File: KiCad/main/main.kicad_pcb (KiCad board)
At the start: 2 copper layers, 88 x 90.3 mm, 39 parts, among them J1 Hexpansion-Connector, J2 Conn_01x04_Socket, U1 TCA8418, U2 AP3032AKTR, U4 ZD24C64A-XGMT

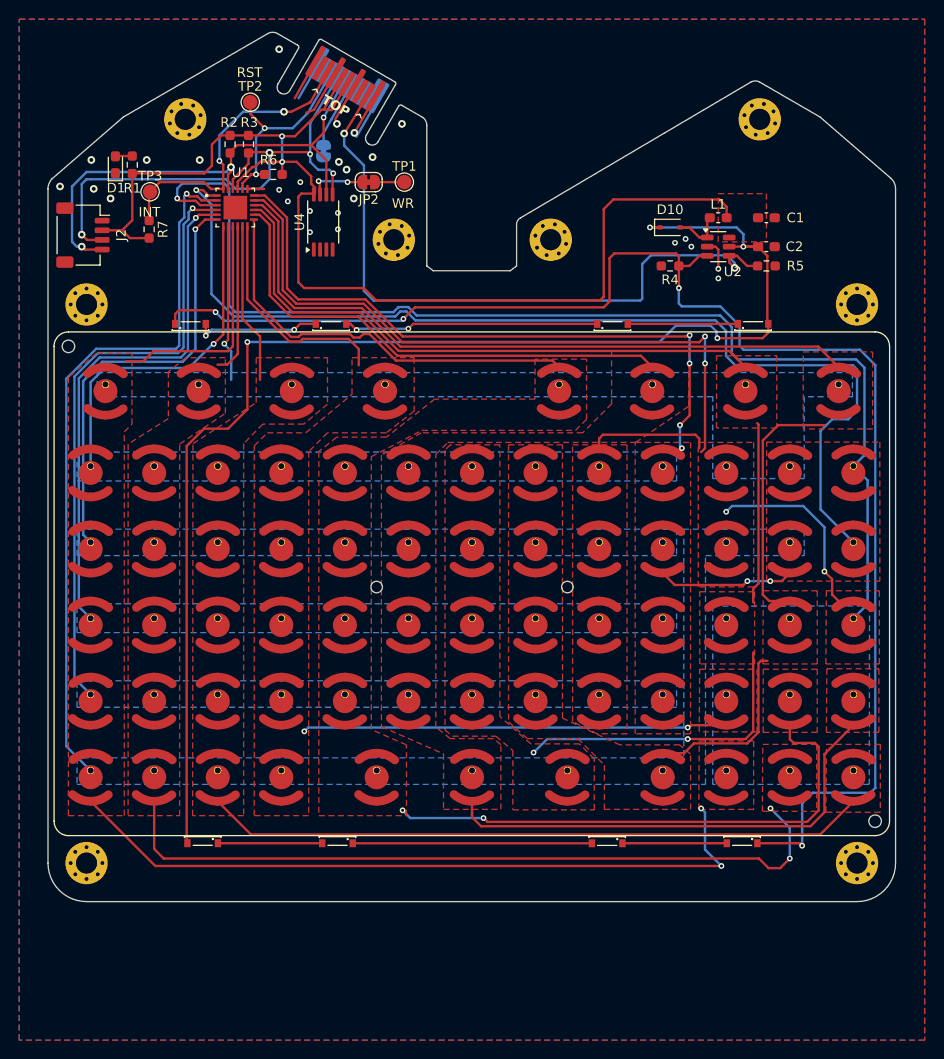
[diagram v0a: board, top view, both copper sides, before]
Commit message: Modify for EMF camp - Change shape - Move standoffs to bottom PCB - Add RGB LEDs and power conversion for them - Add art - Generate and add 3D models
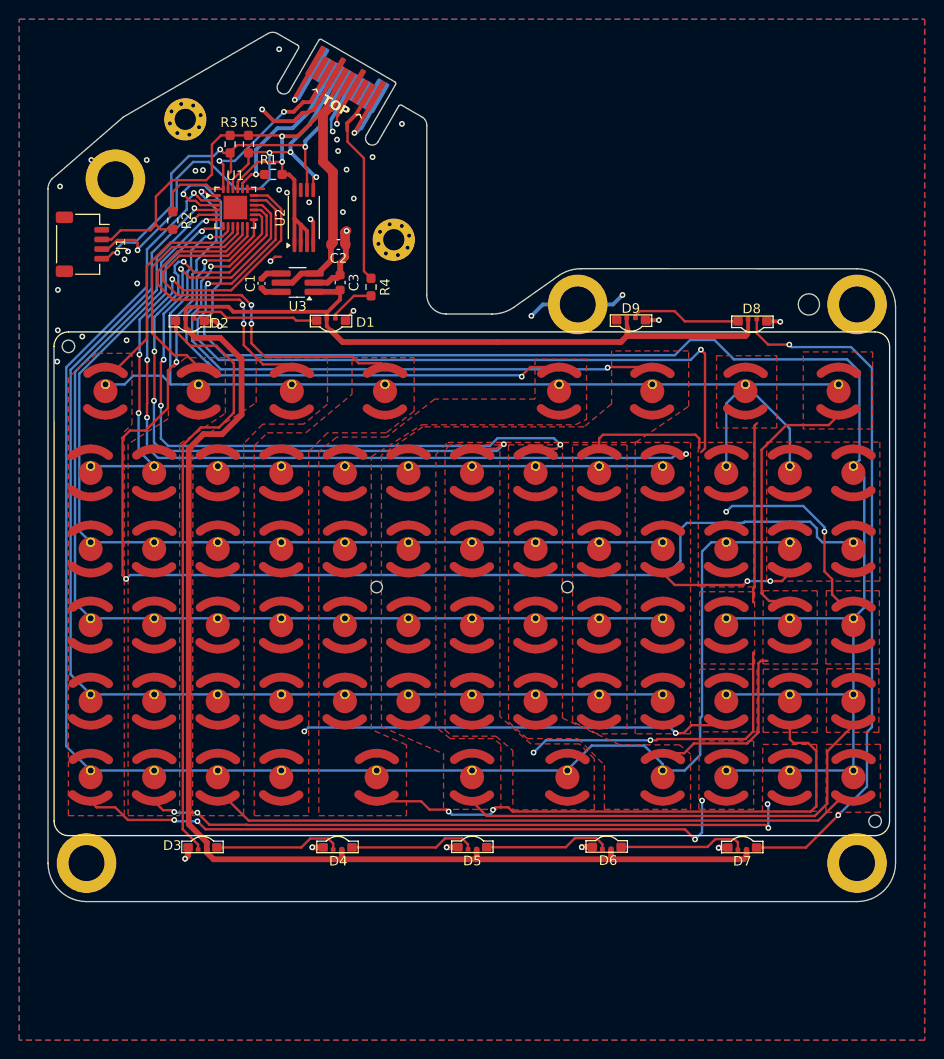
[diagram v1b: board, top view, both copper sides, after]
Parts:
- removed D10: 1N5819WS, Diode_SMD:D_SOD-323
- removed the H3 at (8.20, -35.7)
- removed H8: MountingHole_Pad, MountingHole:MountingHole_2.2mm_M2_Pad_Via
- removed JP1, JP2: SolderJumper_2_Bridged, Jumper:SolderJumper-2_P1.3mm_Bridged_RoundedPad1.0x1.5mm
- removed L1: 6.8uH, Inductor_SMD:L_0603_1608Metric_Pad1.05x0.95mm_HandSolder
- removed the R1 at (-35.2, -43.5)
- removed the R5 at (30.6, -33.0)
- removed TP1, TP2, TP3: TestPoint, TestPoint:TestPoint_Pad_D1.5mm
- removed the U2 at (25.6, -35.0)
- added C3: 10uF, Capacitor_SMD:C_0603_1608Metric, F.Cu at (-13.7, -31.3)
- added H2: SMTSO2020CTJ, frontplate:SMTSO2020CTJ, F.Cu at (11.0, -29.0)
- added U3: AP3602A, Package_TO_SOT_SMD:TSOT-23-6_HandSoldering, F.Cu at (-18.1, -31.3)
- C1: value 10uF -> 1uF; footprint Capacitor_SMD:C_0603_1608Metric_Pad1.08x0.95mm_HandSolder -> Capacitor_SMD:C_0402_1005Metric
- C2: value 1uF -> 10uF; footprint Capacitor_SMD:C_0603_1608Metric_Pad1.08x0.95mm_HandSolder -> Capacitor_SMD:C_0603_1608Metric
- D1: value LED -> XL-3210RGBC-WS2812B; footprint LED_SMD:LED_0603_1608Metric_Pad1.05x0.95mm_HandSolder -> tildagon:XL-3210RGBC-2812B
- D2, D3, D4, D5, D6, D7, D8, D9: value LED -> XL-3210RGBC-WS2812B; footprint keyboard_leds:LTW-010DCG -> tildagon:XL-3210RGBC-2812B
- H4, H5, H6, H7: value MountingHole_Pad -> SMTSO2020CTJ; footprint MountingHole:MountingHole_2.2mm_M2_Pad_Via -> frontplate:SMTSO2020CTJ
- R4: value 20R -> 3k3
- U1: footprint TCA8418RTWR:QFN50P400X400X80-25N -> Package_DFN_QFN:WQFN-24-1EP_4x4mm_P0.5mm_EP2.45x2.45mm
- moved H6 98.8 mm to (-40.0, 29.0)
- moved H5 80.0 mm to (40.0, -29.0)
- moved D9 70.1 mm to (16.5, -27.4)
- moved D8 69.2 mm to (29.1, -27.2)
- moved H4 67.2 mm to (-37.0, -42.0), turned to 0 degrees
- moved D5 61.6 mm to (0.06, 27.4)
- moved D4 61.3 mm to (-13.9, 27.4)
- moved D3 55.9 mm to (-28.0, 27.4)
- moved C1 52.9 mm to (-21.8, -31.2), turned to 90 degrees
- moved C2 44.4 mm to (-13.8, -35.2), turned to 180 degrees
- moved R4 31.1 mm to (-10.5, -30.8), turned to 90 degrees
- moved D1 27.6 mm to (-14.6, -27.3), turned to 180 degrees
- moved D6 14.1 mm to (14.0, 27.3), turned to 0 degrees
- moved D7 14.0 mm to (28.1, 27.4), turned to 0 degrees
- moved R2 2.63 mm to (-31.0, -37.7)
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- renumbered H2 to H3, J2 to J1, J1 to J2, R6 to R1, R7 to R2, R2 to R3, R3 to R5, U4 to U2
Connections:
- C1 pad 1: VCC -> Net-(U3-C+)
- C1 pad 2: GND -> Net-(U3-C-)
- C2 pad 1: VDD -> GND
- C2 pad 2: GND -> VCC
- D1 pad 2: Net-(D1-A) -> Net-(D1-DIN)
- D2 pad 1: Net-(D2-K) -> GND
- D2 pad 2: Net-(D2-A) -> Net-(D1-DOUT)
- D3 pad 1: Net-(D2-A) -> GND
- D3 pad 2: Net-(D3-A) -> Net-(D2-DOUT)
- D4 pad 1: Net-(D3-A) -> GND
- D4 pad 2: Net-(D4-A) -> Net-(D3-DOUT)
- D5 pad 1: Net-(D4-A) -> GND
- D5 pad 2: VDD -> Net-(D4-DOUT)
- D6 pad 1: Net-(D2-K) -> GND
- D6 pad 2: Net-(D6-A) -> Net-(D5-DOUT)
- D7 pad 1: Net-(D6-A) -> GND
- D7 pad 2: Net-(D7-A) -> Net-(D6-DOUT)
- D8 pad 1: Net-(D7-A) -> GND
- D8 pad 2: Net-(D8-A) -> Net-(D7-DOUT)
- D9 pad 1: Net-(D8-A) -> GND
- D9 pad 2: VDD -> Net-(D8-DOUT)
- J2 pad 12: LED_CTRL -> /LED_DATA
- J2 pad 6: Net-(J1-HEXP_DET) -> GND
- R4 pad 1: Net-(D2-K) -> Net-(D1-DIN)
- R4 pad 2: GND -> /LED_DATA
- U2 pad 1: unconnected-(U4-A0-Pad1) -> VCC
- U2 pad 2: unconnected-(U4-A1-Pad2) -> VCC
- U2 pad 3: unconnected-(U4-A2-Pad3) -> VCC
- U2 pad 7: Net-(JP2-B) -> unconnected-(U2-WP-Pad7)
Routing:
- net /5V: track 0.00 -> 195.1 mm
- net Net-(D2-K): track 153.5 -> 0.00 mm, vias 4 -> 0
- net VDD: track 137.4 -> 0.00 mm, vias 4 -> 0
- net /ROW0: track 16.4 -> 116.5 mm
- net /ROW5: track 74.4 -> 166.4 mm
- net Net-(D7-DOUT): track 0.00 -> 72.7 mm, vias 0 -> 2
- net LED_CTRL: track 70.5 -> 0.00 mm, vias 2 -> 0
- net Net-(D2-DOUT): track 0.00 -> 63.0 mm
- net /ROW2: track 45.1 -> 100.1 mm
- net /ROW6: track 121.8 -> 176.7 mm
- net /ROW3: track 54.4 -> 109.1 mm
- net /ROW4: track 63.7 -> 118.5 mm
- net /ROW1: track 35.8 -> 89.9 mm, vias 1 -> 3
- net GND: track 32.3 -> 75.4 mm, vias 26 -> 43
- net VCC: track 125.7 -> 88.1 mm
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- removed copper zone on B.Cu, net /ROW0
- removed copper zone on B.Cu, net /ROW1
- removed copper zone on B.Cu, net /ROW2
- removed copper zone on B.Cu, net /ROW3
- removed copper zone on B.Cu, net /ROW4
- removed copper zone on B.Cu, net /ROW5
- removed copper zone on B.Cu, net /ROW6
- removed copper zone on F.Cu, net VCC
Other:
- outline, holes or cut-outs redrawn
- board text added: "Design by davedarko"
- board text added: "Designed for EMF Camp 2026"
- board text added: "Keeb"
- board text added: "Keypad by Solder Party"
- board text added: "Layout by Kliment"
- board text added: "PCB and assembly:"
- board text added: "Software by sodoku"
- board text added: "TCA8418 by:"
- board text added: "Tildagon"
- board text added: "dex"
- board text added: "for"
- board text added: "pan"
- board text added: "sion"
- board text removed: "INT"
- board text removed: "RST"
- board text removed: "WR"
